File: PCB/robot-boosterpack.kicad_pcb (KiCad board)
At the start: 2 copper layers, 60 x 101 mm, 61 parts, among them IC1 DRV8833, IC2 TPS77033, IC3 TPS77050, IC4 LMR61428, J1 3.3V, J2 5V, J3 9V, M1 MOTOR, M2 MOTOR

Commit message: Rev 1.1
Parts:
- added D5: DIODESCH, DO-214AA(SMB), B.Cu at (204.5, 111.5)
- C2: value 2.2 uF -> 2.2 uF 6.3V
- C4: value 2.2uF -> 2.2uF 6.3V
- C5: value 0.01uF -> 0.01uF 16V X7R
- C6, C7: value 4.7 uF -> 4.7 uF ESR 0.2
- CONN2: value BATTERY -> 3AAA-BATTERY
- CONN3: value DISTANCE -> IR
- J1: value 3.3V -> 3.3V Jumper
- J2: value 5V -> 5V Jumper
- J3: value 9V -> 9V Jumper
- R16: value 165 -> 330
- R17: value 261 -> 520
- R18: value 453 -> 900
- moved R12 3.04 mm to (215.5, 157.5)
- moved R13 2.24 mm to (211.0, 154.0)
- moved IR2 2.06 mm to (189.0, 157.5), turned to 0 degrees
- moved IR4 2.06 mm to (211.0, 157.5), turned to 0 degrees
- moved R14 1.12 mm to (226.0, 152.0)
- moved R15 1.12 mm to (226.0, 154.0)
- moved M1 1.00 mm to (195.0, 64.5), turned to 0 degrees
- moved M2 1.00 mm to (205.0, 64.5)
- moved R11 1.00 mm to (195.5, 157.0)
- moved R6 1.00 mm to (193.5, 157.0)
- moved IR1 0.71 mm to (174.0, 157.5), turned to 0 degrees
- moved IR5 0.71 mm to (226.0, 157.5), turned to 0 degrees
- moved G*** 0.50 mm to (200.0, 74.5)
- moved GEARMOTOR 0.50 mm to (175.0, 83.5)
- moved GEARMOTOR 0.50 mm to (225.0, 65.5)
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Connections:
- C3 pad 1: +9V -> N-0000067
- IC3 pad 1: +9V -> N-0000067
- R10 pad 2: +9V -> N-0000067
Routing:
- net GND: track 301.8 -> 242.5 mm, vias 7 -> 5
- net N-0000059: track 35.5 -> 23.8 mm
- net N-0000067: track 0.00 -> 6.71 mm
- net /IR4: track 91.4 -> 85.8 mm
- net +9V: track 113.7 -> 109.1 mm
- net +3.3V: track 202.1 -> 198.7 mm
- net /IR3: track 72.4 -> 69.0 mm
- net N-0000058: track 25.8 -> 23.3 mm
- net /IR2: track 65.8 -> 67.7 mm
- net /IR1: track 58.5 -> 60.1 mm
- net /IR5: track 90.7 -> 92.0 mm
- net N-0000032: track 9.21 -> 7.90 mm
- net N-0000057: track 25.0 -> 24.0 mm
- net N-0000056: track 25.0 -> 24.0 mm
- net N-000007: track 3.36 -> 2.81 mm
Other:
- board size 60 x 101 mm -> 60 x 100 mm
- board text added: "1"

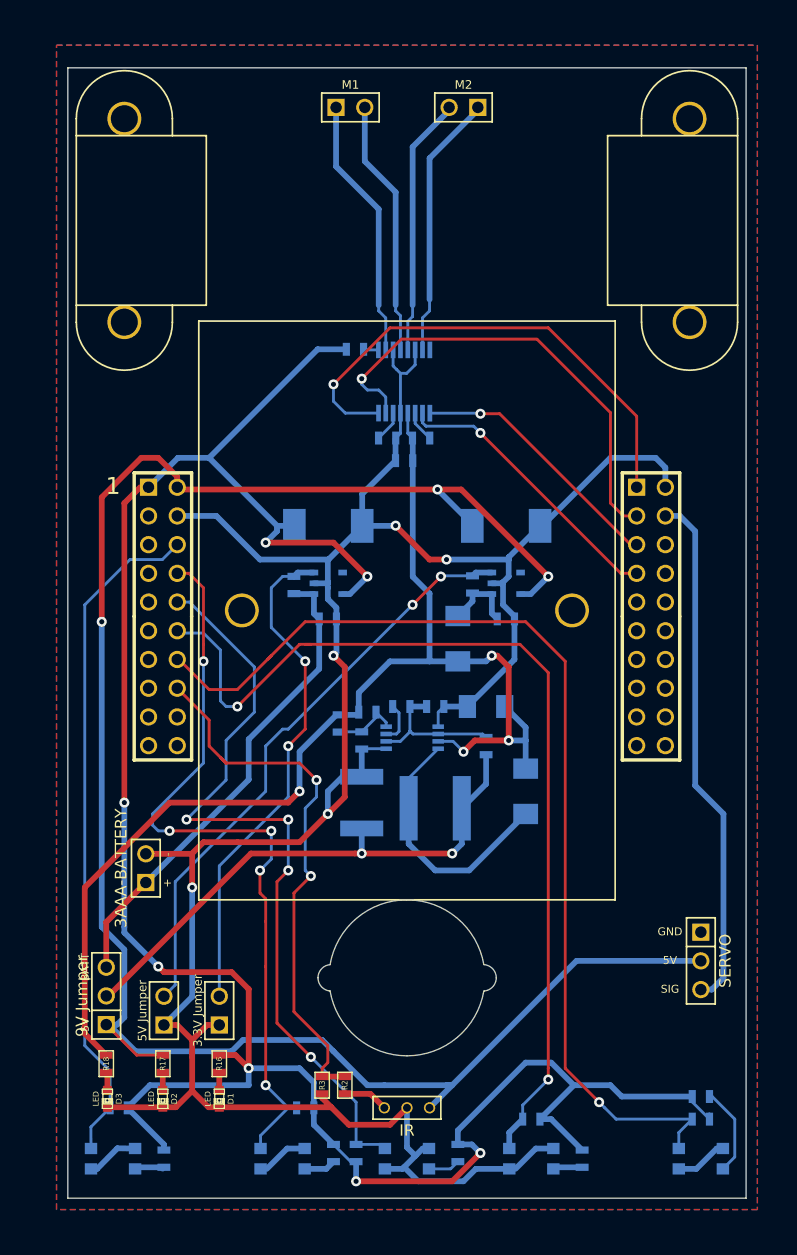
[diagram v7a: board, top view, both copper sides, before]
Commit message: Fixes for unupdated ground plane!
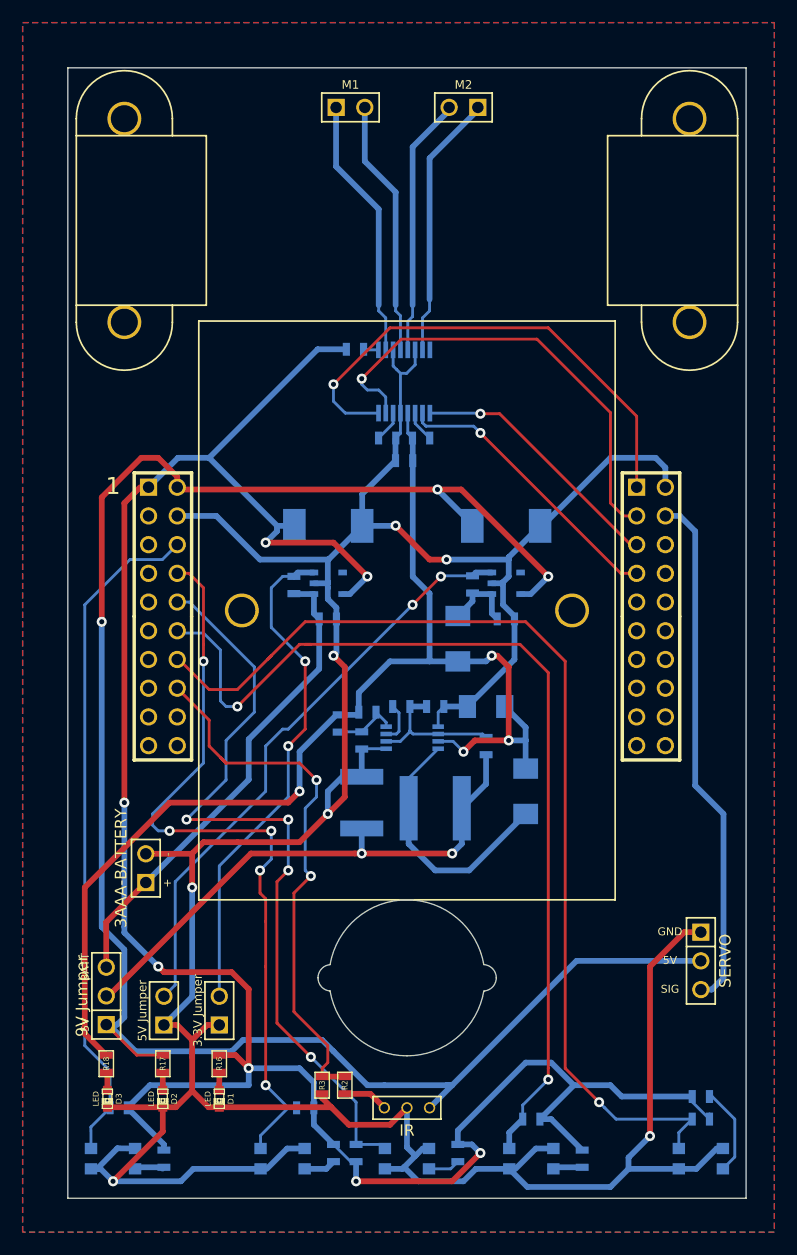
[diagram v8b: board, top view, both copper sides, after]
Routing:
- net GND: track 242.5 -> 307.6 mm, vias 5 -> 7
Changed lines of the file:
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@@
     (thickness 1.6)
     (drawings 36)
-    (tracks 540)
+    (tracks 558)
     (zones 0)
     (modules 62)
@@
   )
   (setup
-    (last_trace_width 0.508)
+    (last_trace_width 0.254)
     (user_trace_width 0.508)
     (user_trace_width 0.762)
@@
     (pad_to_mask_clearance 0)
     (aux_axis_origin 0 0)
-    (visible_elements 7FFFFFFF)
+    (visible_elements 7FFFFBFF)
     (pcbplotparams
       (layerselection 284196865)
@@
   (segment (start 228 141.5) (end 228 127) (width 0.508) (layer B.Cu) (net 15))
   (segment (start 226.96 142.54) (end 228 141.5) (width 0.508) (layer B.Cu) (net 15))
-  (segment (start 209.05 158.4) (end 206.1 158.4) (width 0.508) (layer B.Cu) (net 16) (status 400000))
-  (segment (start 201 159.5) (end 199.75 158.25) (width 0.508) (layer B.Cu) (net 16))
-  (segment (start 205 159.5) (end 201 159.5) (width 0.508) (layer B.Cu) (net 16))
+  (segment (start 226 137.46) (end 224.54 137.46) (width 0.508) (layer F.Cu) (net 16))
+  (segment (start 219.6 157.4) (end 219.6 158.4) (width 0.508) (layer B.Cu) (net 16))
+  (segment (start 221.5 155.5) (end 219.6 157.4) (width 0.508) (layer B.Cu) (net 16))
+  (via (at 221.5 155.5) (size 0.889) (layers F.Cu B.Cu) (net 16))
+  (segment (start 221.5 140.5) (end 221.5 155.5) (width 0.508) (layer F.Cu) (net 16))
+  (segment (start 224.54 137.46) (end 221.5 140.5) (width 0.508) (layer F.Cu) (net 16))
+  (segment (start 224.05 158.4) (end 219.6 158.4) (width 0.508) (layer B.Cu) (net 16))
+  (segment (start 210.65 160) (end 209.05 158.4) (width 0.508) (layer B.Cu) (net 16))
+  (segment (start 218 160) (end 210.65 160) (width 0.508) (layer B.Cu) (net 16))
+  (segment (start 219.6 158.4) (end 218 160) (width 0.508) (layer B.Cu) (net 16))
+  (segment (start 187.05 158.4) (end 181.1 158.4) (width 0.508) (layer B.Cu) (net 16))
+  (segment (start 180 159.5) (end 174 159.5) (width 0.508) (layer B.Cu) (net 16))
+  (segment (start 181.1 158.4) (end 180 159.5) (width 0.508) (layer B.Cu) (net 16))
+  (segment (start 172.05 158.4) (end 172.9 158.4) (width 0.508) (layer B.Cu) (net 16))
+  (segment (start 172.9 158.4) (end 174 159.5) (width 0.508) (layer B.Cu) (net 16))
+  (segment (start 178.4 155.1) (end 178.4 152.9493) (width 0.508) (layer F.Cu) (net 16))
+  (via (at 174 159.5) (size 0.889) (layers F.Cu B.Cu) (net 16))
+  (segment (start 174 159.5) (end 178.4 155.1) (width 0.508) (layer F.Cu) (net 16))
+  (segment (start 209.05 158.4) (end 206.1 158.4) (width 0.508) (layer B.Cu) (net 16))
   (segment (start 206.1 158.4) (end 205 159.5) (width 0.508) (layer B.Cu) (net 16))
+  (segment (start 205 159.5) (end 201 159.5) (width 0.508) (layer B.Cu) (net 16))
+  (segment (start 201 159.5) (end 199.75 158.25) (width 0.508) (layer B.Cu) (net 16))
   (segment (start 227.95 156.6) (end 227.4 156.6) (width 0.508) (layer B.Cu) (net 16))
   (segment (start 225.6 158.4) (end 224.05 158.4) (width 0.508) (layer B.Cu) (net 16))
   (segment (start 227.4 156.6) (end 225.6 158.4) (width 0.508) (layer B.Cu) (net 16))
   (segment (start 209.05 158.4) (end 209.6 158.4) (width 0.254) (layer B.Cu) (net 16))
-  (segment (start 211.4 156.6) (end 212.95 156.6) (width 0.508) (layer B.Cu) (net 16))
   (segment (start 209.6 158.4) (end 211.4 156.6) (width 0.508) (layer B.Cu) (net 16))
+  (segment (start 211.4 156.6) (end 212.95 156.6) (width 0.508) (layer B.Cu) (net 16))
   (segment (start 200 153) (end 200 156.5) (width 0.508) (layer B.Cu) (net 16))
   (segment (start 200 156.5) (end 200.75 157.25) (width 0.508) (layer B.Cu) (net 16))
@@
   (segment (start 190.95 158.4) (end 192.862 158.4) (width 0.508) (layer B.Cu) (net 40))
   (segment (start 192.862 158.4) (end 193.5 157.762) (width 0.508) (layer B.Cu) (net 40))
-  (zone (net 16) (net_name GND) (layer F.Cu) (hatch edge 0.508)
+  (zone (net 16) (net_name GND) (layer B.Cu) (hatch edge 0.508)
     (connect_pads (clearance 0.508))
     (min_thickness 0.254)
@@
     (polygon
       (pts
-        (xy 231 162) (xy 169 162) (xy 169 59) (xy 231 59)
+        (xy 232.5 164) (xy 166 164) (xy 166 57) (xy 232.5 57)
       )
     )
   )
-  (zone (net 16) (net_name GND) (layer B.Cu) (hatch edge 0.508)
+  (zone (net 16) (net_name GND) (layer F.Cu) (hatch edge 0.508)
     (connect_pads (clearance 0.508))
     (min_thickness 0.254)
@@
     (polygon
       (pts
-        (xy 231 162) (xy 169 162) (xy 169 59) (xy 231 59)
+        (xy 232.5 164) (xy 166 164) (xy 166 57) (xy 232.5 57)
       )
     )
